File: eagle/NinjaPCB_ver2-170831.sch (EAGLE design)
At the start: 76 parts, among them IC2 VNH5019/VNH3SP30-BNC, IC3 ANALOGSW_AD_SOT23-6NC, IC4 ANALOGSW_TI-SC70-5/6NC, IC5 MCP3551SNNC, IC6 NAU7802NC, J2 ATX24, J3 HEATER, J4 HEATER_TEMP, J5 PELTIER, Q2 IRF520NPBF, Q3 IRF520NPBF, U1 CJT1117-3.3-SOT223

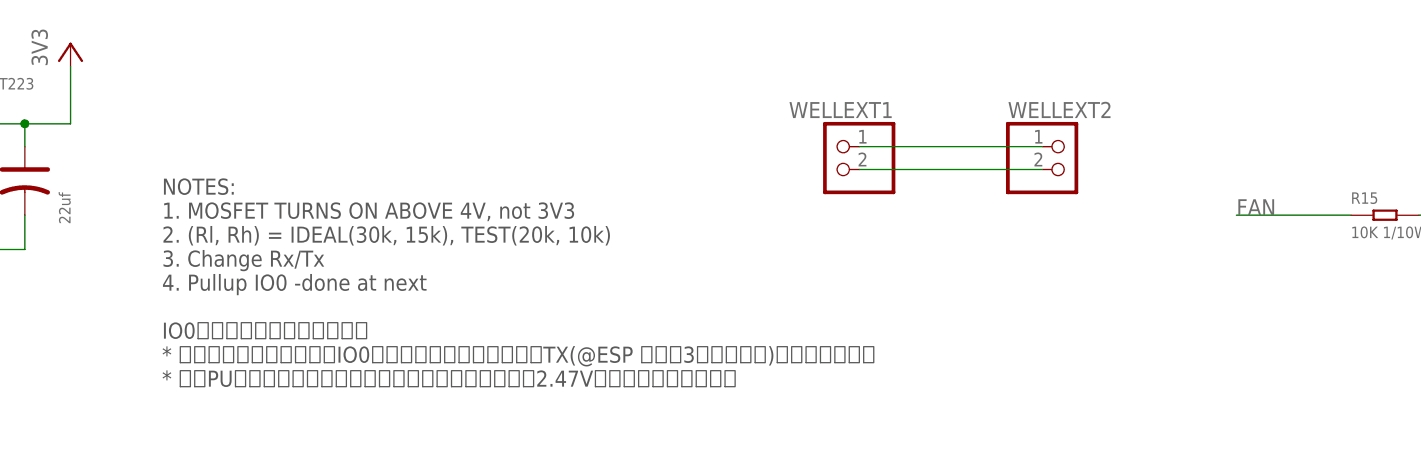
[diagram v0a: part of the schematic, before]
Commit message: pulldown HEATER to write
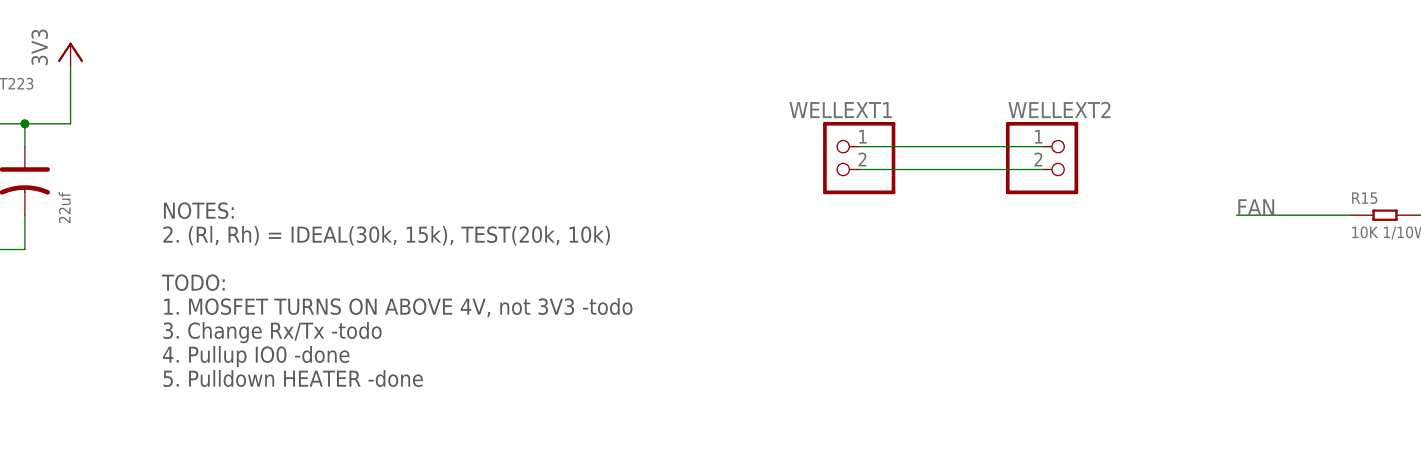
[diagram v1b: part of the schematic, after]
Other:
- note added: "NOTES: 2. (Rl, Rh) = IDEAL(30k, 15k), TEST(20k, 10k) TODO: 1. MOSFET TURNS ON ABOVE 4V, not 3V3 -todo 3. Change Rx/Tx -todo 4. Pullup IO0 -done 5. Pulldown HEATER -done"
- note removed: "NOTES: 1. MOSFET TURNS ON ABOVE 4V, not 3V3 2. (Rl, Rh) = IDEAL(30k, 15k), TEST(20k, 10k) 3. Change Rx/Tx 4. Pullup IO0 -done at next IO0の接続がなんだかあやしい * 電源を入れた状態だと、IO0ボタンを押しても離してもTX(@ESP 端から3番目のピン)と導通している * 本来PUされているはずなのだがボタンを離した状態で2.47Vという中途半端な電圧"
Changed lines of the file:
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@@
 <text x="38.1" y="77.47" size="3.81" layer="97">POWER</text>
 <text x="171.45" y="26.67" size="1.778" layer="97">NOTES:
-1. MOSFET TURNS ON ABOVE 4V, not 3V3
 2. (Rl, Rh) = IDEAL(30k, 15k), TEST(20k, 10k)
-3. Change Rx/Tx
-4. Pullup IO0 -done at next
-IO0の接続がなんだかあやしい
-* 電源を入れた状態だと、IO0ボタンを押しても離してもTX(@ESP 端から3番目のピン)と導通している
-* 本来PUされているはずなのだがボタンを離した状態で2.47Vという中途半端な電圧</text>
+TODO:
+1. MOSFET TURNS ON ABOVE 4V, not 3V3 -todo
+3. Change Rx/Tx -todo
+4. Pullup IO0 -done
+5. Pulldown HEATER -done</text>
 </plain>
 <instances>

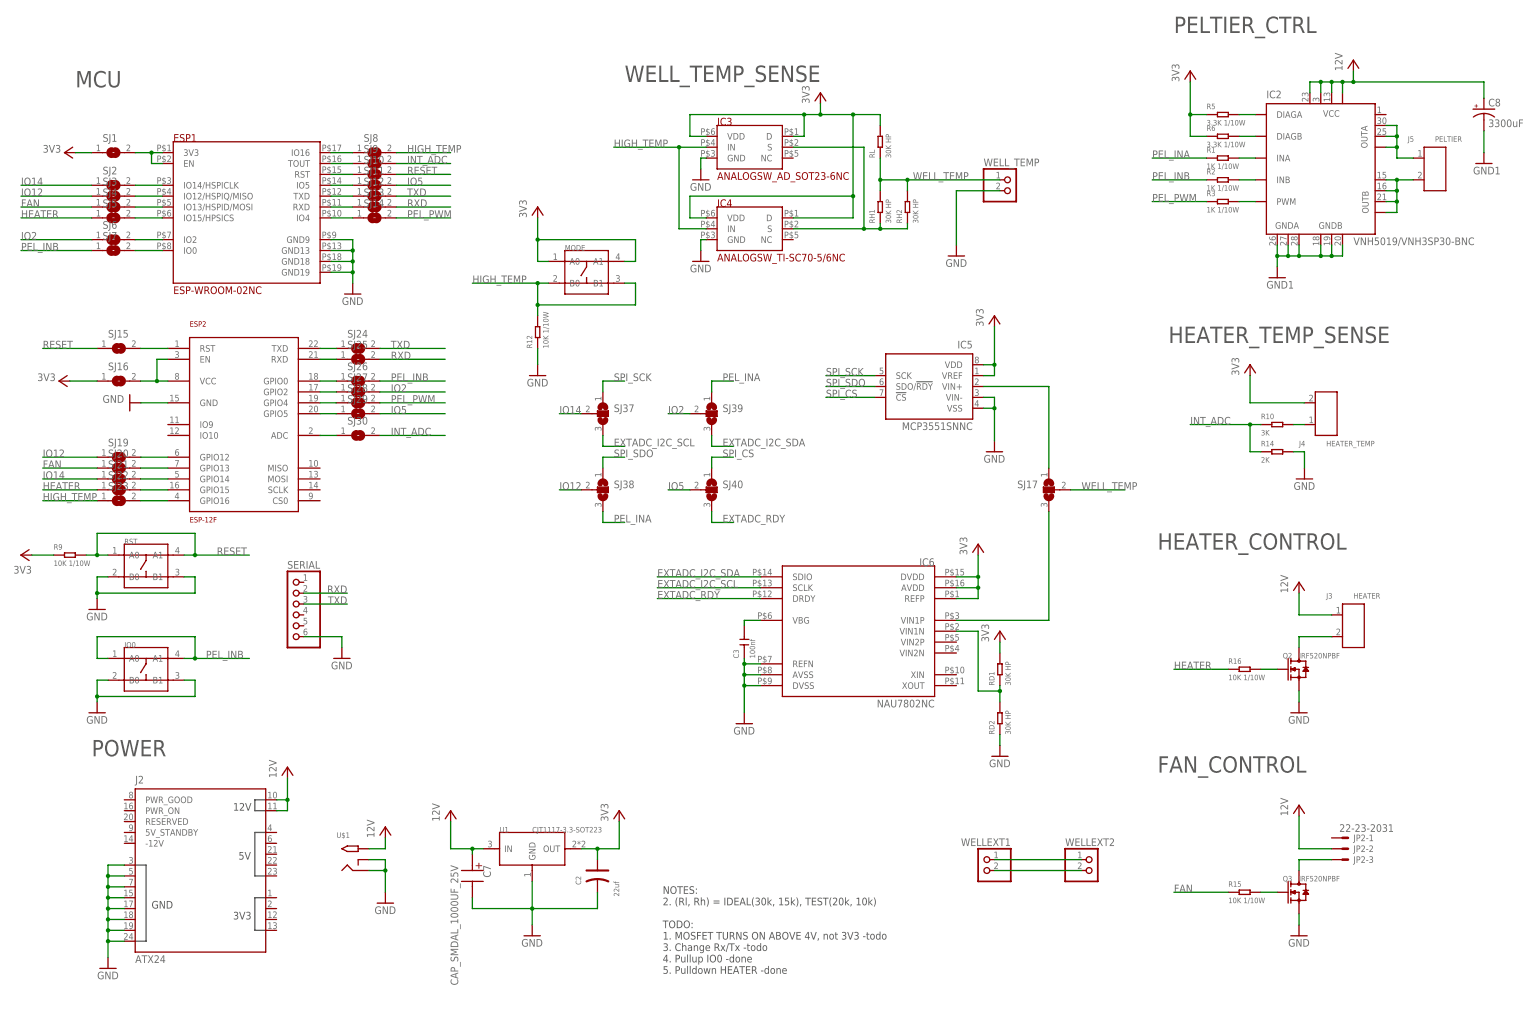
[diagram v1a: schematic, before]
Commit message: VNH5019 doesnot have same pinout as VNH3SP30
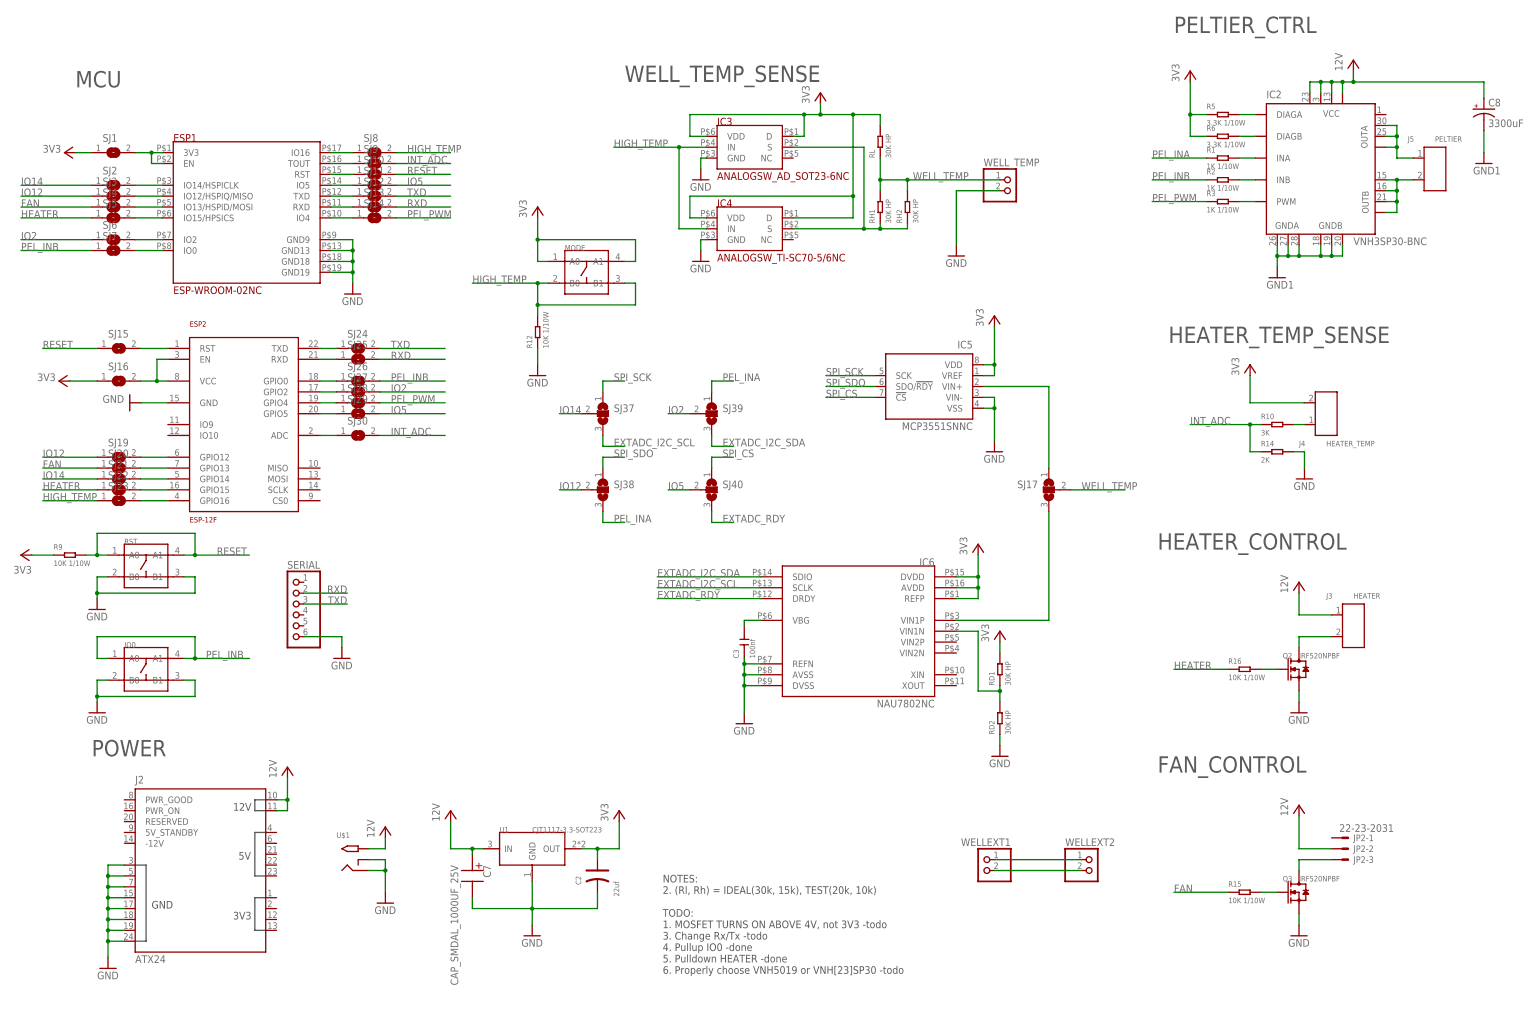
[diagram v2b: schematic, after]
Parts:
- IC2: value VNH5019/VNH3SP30-BNC -> VNH3SP30-BNC; device st-microelectronics:VNH5019/VNH3SP30-BNC -> st-microelectronics:VNH3SP30-BNC
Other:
- note added: "NOTES: 2. (Rl, Rh) = IDEAL(30k, 15k), TEST(20k, 10k) TODO: 1. MOSFET TURNS ON ABOVE 4V, not 3V3 -todo 3. Change Rx/Tx -todo 4. Pullup IO0 -done 5. Pulldown HEATER -done 6. Properly choose VNH5019 or VNH[23]SP30 -todo"
- note removed: "NOTES: 2. (Rl, Rh) = IDEAL(30k, 15k), TEST(20k, 10k) TODO: 1. MOSFET TURNS ON ABOVE 4V, not 3V3 -todo 3. Change Rx/Tx -todo 4. Pullup IO0 -done 5. Pulldown HEATER -done"
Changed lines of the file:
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@@
 <part name="GND21" library="openpcr" deviceset="GND1" device=""/>
 <part name="SJ17" library="jumper" deviceset="SJ2W" device=""/>
-<part name="IC2" library="st-microelectronics" deviceset="VNH5019/VNH3SP30-B" device="NC" value="VNH5019/VNH3SP30-BNC"/>
+<part name="IC2" library="st-microelectronics" deviceset="VNH3SP30-B" device="NC" value="VNH3SP30-BNC"/>
 <part name="U$1" library="adafruit" deviceset="2.1MMJACK" device="THM"/>
 <part name="RH2" library="PCR-RCL" deviceset="R0603" device="NC" value="30K HP"/>
@@
 3. Change Rx/Tx -todo
 4. Pullup IO0 -done
-5. Pulldown HEATER -done</text>
+5. Pulldown HEATER -done
+6. Properly choose VNH5019 or VNH[23]SP30 -todo</text>
 </plain>
 <instances>
